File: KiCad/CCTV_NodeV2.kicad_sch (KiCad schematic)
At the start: 9 parts, among them J1 Solar 6V/10W, J2 Battery (ext, 2× 18650 ||), U1 CN3791, U2 TC4056A_BMS, U3 MT3608, U4 ESP32-S3-DevKitC-1 N16R8, U5 OV7670

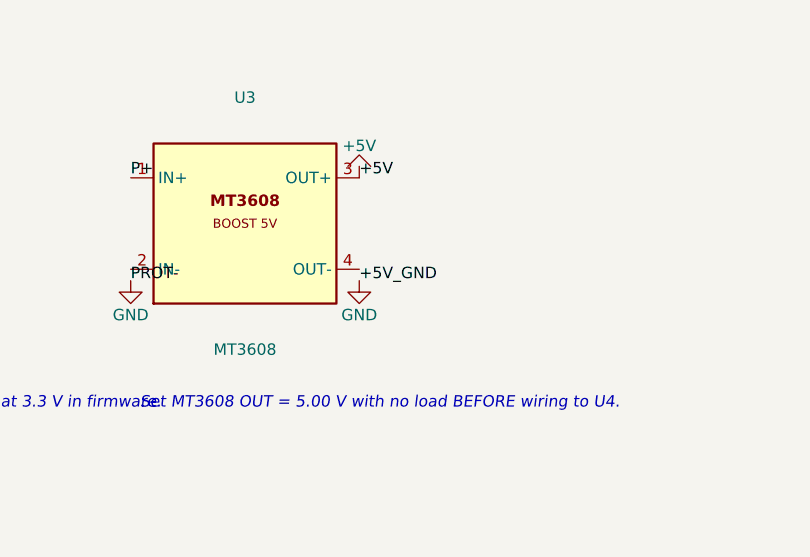
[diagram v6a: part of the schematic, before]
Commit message: Fix U3 MT3608 pad 4: remove '+5V_GND' net, correct to GND
OUT- of a boost converter is the output return path = GND.
A net label '+5V_GND' had been placed at the MT3608 OUT- pin
position (192.7, 75.08) in the schematic, causing KiCad to create
a merged '/+5V_GND' net that incorrectly tied the +5V and GND
buses together on pad 4.

Schematic (CCTV_NodeV2.kicad_sch):
- Deleted stray net label '+5V_GND' at (192.7, 75.08)
- The GND power symbol already present at (192.7, 76.35)
  connects OUT- to GND correctly — no replacement needed

PCB (CCTV_NodeV2.kicad_pcb):
- U3 pad 4 (OUT-): net '/+5V_GND' → 'GND'
- This removes the short circuit between +5V and GND on U3
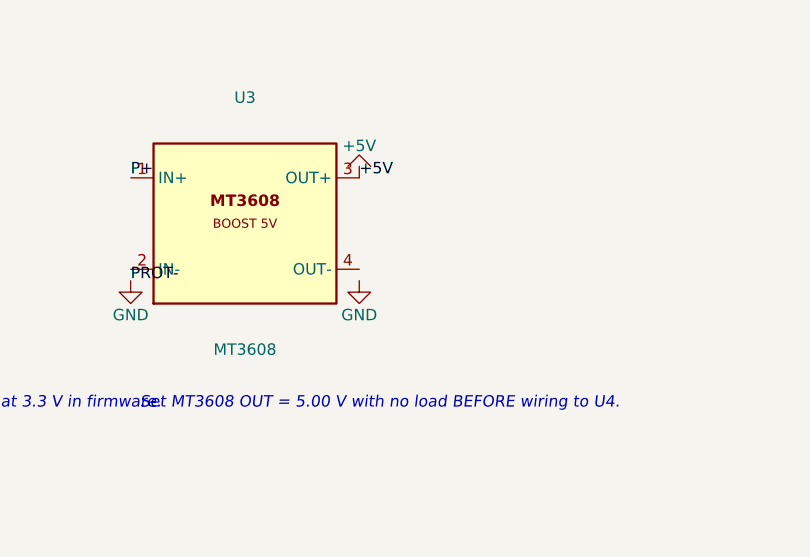
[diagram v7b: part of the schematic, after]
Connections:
- net +5V_GND: no longer names the net of U3.4 (OUT-)
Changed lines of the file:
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@@
 		(effects (font (size 1.27 1.27)) (justify left bottom))
-	)
-	(label "+5V_GND"
-		(at 192.7 75.08 0)
-		(effects (font (size 1.27 1.27)) (justify left top))
 	)
 	(label "P+"

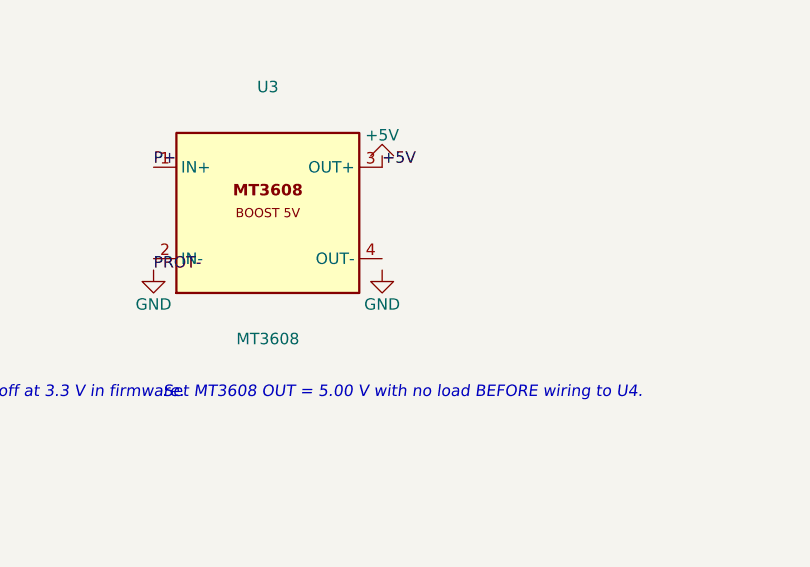
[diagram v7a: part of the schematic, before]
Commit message: Fix U3 MT3608 pad 4 (OUT-): GND → PROT- (same node as pad 2 IN-)
Pad 2 (IN-) and pad 4 (OUT-) of the MT3608 module are connected
together on the module's internal copper pour — they are the SAME
electrical node. Both must be on the PROT- net so the BMS can
actually cut off the load when over-discharge occurs.

Previously pad 4 was changed to GND in the last commit, which would
have shorted the BMS protection FETs (PROT- → GND directly) and
made the DW01A protection circuit useless.

Correct circuit:
  Battery B- → BMS B- → [DW01A FETs] → PROT- → MT3608 pad2(IN-)
                                                         ↕ (same node on module PCB)
                                               PROT- → MT3608 pad4(OUT-)
                                                         ↓
                                               PROT- → ESP32 GND / all load GND

When BMS trips at ~2.4V: PROT- floats → MT3608 loses return path
→ output collapses → ESP32 off. ✓

Schematic: replaced GND power symbol at MT3608 OUT- with PROT- label
PCB: U3 pad 4 net GND → /PROT-
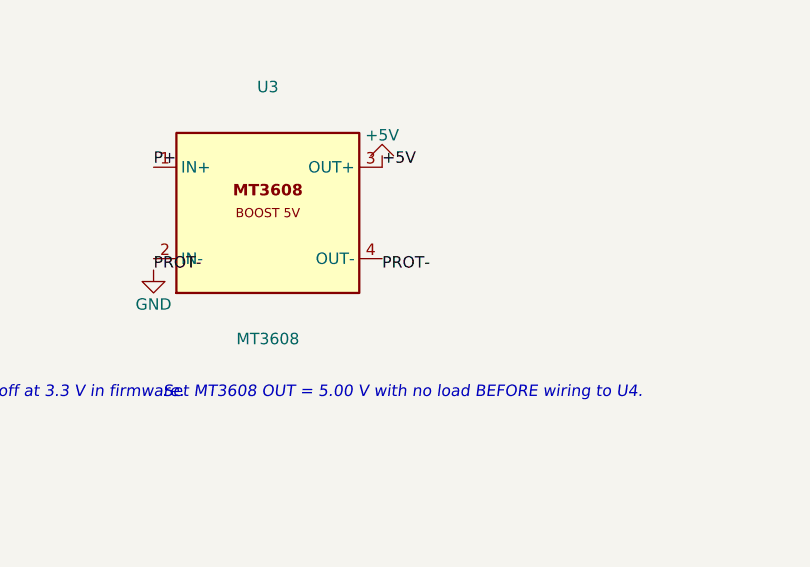
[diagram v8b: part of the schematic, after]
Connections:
- net PROT-: now also U3.4 (OUT-)
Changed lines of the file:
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@@
 		)
 	)
-	(symbol
-		(lib_id "CCTV2:GND")
-		(at 192.7 76.35 0)
-		(unit 1)
-		(in_bom yes)
-		(on_board yes)
-		(dnp no)
-		(property "Reference" "#PWR13"
-			(at 192.7 82.7 0)
-			(hide yes)
-		)
-		(property "Value" "GND"
-			(at 192.7 80.16 0)
-		)
-		(pin "1")
-		(instances
-			(project "CCTV_NodeV2"
-				(path "/b0c0d0e0-0001-4000-8000-000000000001"
-					(reference "#PWR13")
-					(unit 1)
-				)
-			)
-		)
+	(label "PROT-"
+		(at 192.7 75.08 0)
+		(effects (font (size 1.27 1.27)) (justify left top))
+		(uuid "c000000c-new1-0000-0000-000000000001")
 	)
 	(symbol
